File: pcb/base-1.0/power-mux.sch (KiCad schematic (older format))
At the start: 23 parts, among them Q201 IRF7324, Q202 IRF7324, Q203 IRF7324, U201 LTC4417

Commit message: o Replacing footprints with IPC footprints.
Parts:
- C201, C202, C203, C204, C205, C206: footprint Capacitor_SMD:C_0402_1005Metric -> IPC-7351-CAPC:CAPC_1005x015
- R201, R202, R203, R204, R205, R206, R207, R208, R209, R210, R211, R212: footprint Resistor_SMD:R_0402_1005Metric -> IPC-7351-RESC:RESC_1005x015

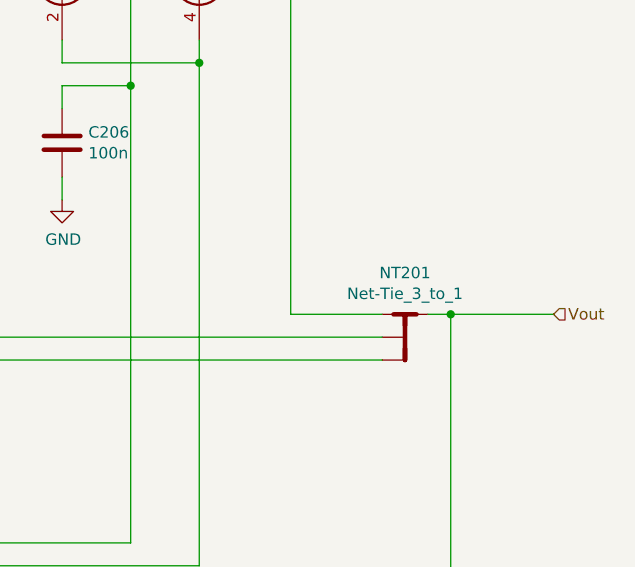
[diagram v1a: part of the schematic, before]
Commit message: o Better symbol for BC817, Q101 and Q102. o Adding footprint for jack, J104.
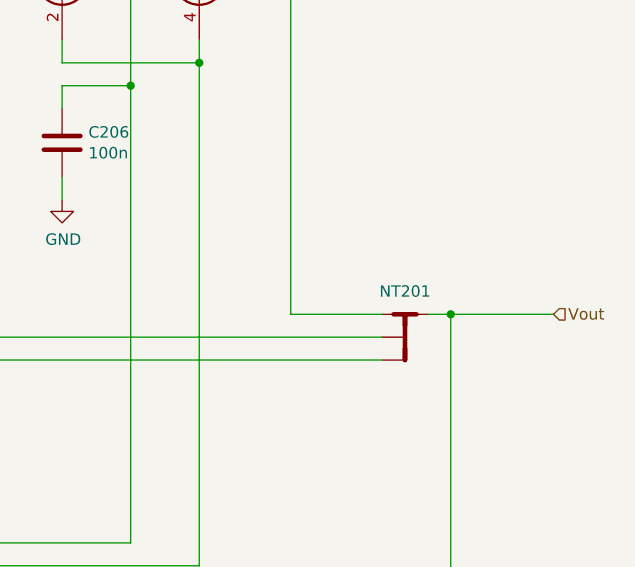
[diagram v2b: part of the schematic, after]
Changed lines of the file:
@@
 U 1 1 5D02029B
 P 10000 3400
-F 0 "NT201" H 10000 3581 50  0000 C CNN
-F 1 "Net-Tie_3_to_1" H 10000 3490 50  0000 C CNN
+F 0 "NT201" H 10000 3500 50  0000 C CNN
+F 1 "Net-Tie_3_to_1" H 10000 3490 50  0001 C CNN
 F 2 "NetTie:NetTie-4_SMD_Pad0.5mm" H 10000 3400 50  0001 C CNN
 F 3 "~" H 10000 3400 50  0001 C CNN

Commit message: o Selecting parts.
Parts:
- C201, C202, C203, C204, C205, C206: value 100n -> 100nF; mpn (none) -> CL05B104KO5NNNC
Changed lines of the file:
@@
 P 8500 2650
 F 0 "C206" H 8615 2696 50  0000 L CNN
-F 1 "100n" H 8615 2605 50  0000 L CNN
+F 1 "100nF" H 8615 2605 50  0000 L CNN
 F 2 "IPC-7351-CAPC:CAPC_1005x015" H 8538 2500 50  0001 C CNN
 F 3 "~" H 8500 2650 50  0001 C CNN
+F 4 "CL05B104KO5NNNC" H 8500 2650 50  0001 C CNN "mpn"
 	1    8500 2650
 	1    0    0    -1
@@
 P 2300 1600
 F 0 "C202" H 2415 1646 50  0000 L CNN
-F 1 "100n" H 2415 1555 50  0000 L CNN
+F 1 "100nF" H 2415 1555 50  0000 L CNN
 F 2 "IPC-7351-CAPC:CAPC_1005x015" H 2338 1450 50  0001 C CNN
 F 3 "~" H 2300 1600 50  0001 C CNN
+F 4 "CL05B104KO5NNNC" H 2300 1600 50  0001 C CNN "mpn"
 	1    2300 1600
 	1    0    0    -1
@@
 P 1600 1600
 F 0 "C201" H 1715 1646 50  0000 L CNN
-F 1 "100n" H 1715 1555 50  0000 L CNN
+F 1 "100nF" H 1715 1555 50  0000 L CNN
 F 2 "IPC-7351-CAPC:CAPC_1005x015" H 1638 1450 50  0001 C CNN
 F 3 "~" H 1600 1600 50  0001 C CNN
+F 4 "CL05B104KO5NNNC" H 1600 1600 50  0001 C CNN "mpn"
 	1    1600 1600
 	1    0    0    -1
@@
 P 3000 1600
 F 0 "C203" H 3115 1646 50  0000 L CNN
-F 1 "100n" H 3115 1555 50  0000 L CNN
+F 1 "100nF" H 3115 1555 50  0000 L CNN
 F 2 "IPC-7351-CAPC:CAPC_1005x015" H 3038 1450 50  0001 C CNN
 F 3 "~" H 3000 1600 50  0001 C CNN
+F 4 "CL05B104KO5NNNC" H 3000 1600 50  0001 C CNN "mpn"
 	1    3000 1600
 	1    0    0    -1
@@
 P 6700 2650
 F 0 "C205" H 6815 2696 50  0000 L CNN
-F 1 "100n" H 6815 2605 50  0000 L CNN
+F 1 "100nF" H 6815 2605 50  0000 L CNN
 F 2 "IPC-7351-CAPC:CAPC_1005x015" H 6738 2500 50  0001 C CNN
 F 3 "~" H 6700 2650 50  0001 C CNN
+F 4 "CL05B104KO5NNNC" H 6700 2650 50  0001 C CNN "mpn"
 	1    6700 2650
 	1    0    0    -1
@@
 P 4900 2650
 F 0 "C204" H 5015 2696 50  0000 L CNN
-F 1 "100n" H 5015 2605 50  0000 L CNN
+F 1 "100nF" H 5015 2605 50  0000 L CNN
 F 2 "IPC-7351-CAPC:CAPC_1005x015" H 4938 2500 50  0001 C CNN
 F 3 "~" H 4900 2650 50  0001 C CNN
+F 4 "CL05B104KO5NNNC" H 4900 2650 50  0001 C CNN "mpn"
 	1    4900 2650
 	1    0    0    -1

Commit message: o Selecting parts.
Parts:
- Q201, Q202, Q203: value IRF7324 -> IRF7324TRPBF; mpn (none) -> IRF7324TRPBF
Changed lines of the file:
@@
 P 9100 2000
 F 0 "Q203" V 9525 2000 50  0000 C CNN
-F 1 "IRF7324" V 9434 2000 50  0000 C CNN
+F 1 "IRF7324TRPBF" V 9434 2000 50  0000 C CNN
 F 2 "Package_SO:PowerIntegrations_SO-8" H 9150 2000 50  0001 C CNN
-F 3 "~" H 9150 2000 50  0001 C CNN
+F 3 "https://www.infineon.com/dgdl/irf7324pbf.pdf?fileId=5546d462533600a4015355f5f0861b4b" H 9150 2000 50  0001 C CNN
+F 4 "IRF7324TRPBF" H 9100 2000 50  0001 C CNN "mpn"
 	2    9100 2000
 	0    1    -1   0
@@
 P 8500 2000
 F 0 "Q203" V 8925 2000 50  0000 C CNN
-F 1 "IRF7324" V 8834 2000 50  0000 C CNN
+F 1 "IRF7324TRPBF" V 8834 2000 50  0000 C CNN
 F 2 "Package_SO:PowerIntegrations_SO-8" H 8550 2000 50  0001 C CNN
-F 3 "~" H 8550 2000 50  0001 C CNN
+F 3 "https://www.infineon.com/dgdl/irf7324pbf.pdf?fileId=5546d462533600a4015355f5f0861b4b" H 8550 2000 50  0001 C CNN
+F 4 "IRF7324TRPBF" H 8500 2000 50  0001 C CNN "mpn"
 	1    8500 2000
 	0    -1   -1   0
@@
 P 7300 2000
 F 0 "Q202" V 7725 2000 50  0000 C CNN
-F 1 "IRF7324" V 7634 2000 50  0000 C CNN
+F 1 "IRF7324TRPBF" V 7634 2000 50  0000 C CNN
 F 2 "Package_SO:PowerIntegrations_SO-8" H 7350 2000 50  0001 C CNN
-F 3 "~" H 7350 2000 50  0001 C CNN
+F 3 "https://www.infineon.com/dgdl/irf7324pbf.pdf?fileId=5546d462533600a4015355f5f0861b4b" H 7350 2000 50  0001 C CNN
+F 4 "IRF7324TRPBF" H 7300 2000 50  0001 C CNN "mpn"
 	2    7300 2000
 	0    1    -1   0
@@
 P 6700 2000
 F 0 "Q202" V 7125 2000 50  0000 C CNN
-F 1 "IRF7324" V 7034 2000 50  0000 C CNN
+F 1 "IRF7324TRPBF" V 7034 2000 50  0000 C CNN
 F 2 "Package_SO:PowerIntegrations_SO-8" H 6750 2000 50  0001 C CNN
-F 3 "~" H 6750 2000 50  0001 C CNN
+F 3 "https://www.infineon.com/dgdl/irf7324pbf.pdf?fileId=5546d462533600a4015355f5f0861b4b" H 6750 2000 50  0001 C CNN
+F 4 "IRF7324TRPBF" H 6700 2000 50  0001 C CNN "mpn"
 	1    6700 2000
 	0    -1   -1   0
@@
 P 5500 2000
 F 0 "Q201" V 5925 2000 50  0000 C CNN
-F 1 "IRF7324" V 5834 2000 50  0000 C CNN
+F 1 "IRF7324TRPBF" V 5834 2000 50  0000 C CNN
 F 2 "Package_SO:PowerIntegrations_SO-8" H 5550 2000 50  0001 C CNN
-F 3 "~" H 5550 2000 50  0001 C CNN
+F 3 "https://www.infineon.com/dgdl/irf7324pbf.pdf?fileId=5546d462533600a4015355f5f0861b4b" H 5550 2000 50  0001 C CNN
+F 4 "IRF7324TRPBF" H 5500 2000 50  0001 C CNN "mpn"
 	2    5500 2000
 	0    1    -1   0
@@
 P 4900 2000
 F 0 "Q201" V 5325 2000 50  0000 C CNN
-F 1 "IRF7324" V 5234 2000 50  0000 C CNN
+F 1 "IRF7324TRPBF" V 5234 2000 50  0000 C CNN
 F 2 "Package_SO:PowerIntegrations_SO-8" H 4950 2000 50  0001 C CNN
-F 3 "~" H 4950 2000 50  0001 C CNN
+F 3 "https://www.infineon.com/dgdl/irf7324pbf.pdf?fileId=5546d462533600a4015355f5f0861b4b" H 4950 2000 50  0001 C CNN
+F 4 "IRF7324TRPBF" H 4900 2000 50  0001 C CNN "mpn"
 	1    4900 2000
 	0    -1   -1   0

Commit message: o Much more PCB work.
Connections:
- net Vin_PoE_sel: now reaches NT201.1, Q203.5 (D), Q203.6 (D)
- net Vin_adapter_sel: now reaches NT201.2, Q202.5 (D), Q202.6 (D)
- net Vin_USB_sel: now reaches NT201.3, Q201.5 (D), Q201.6 (D)
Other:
- moved on the sheet: NT201
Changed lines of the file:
@@
 TODO:\n* Select MOSFETs. One option: CSD75207W15\n* Calculate resistor values
 Wire Wire Line
-	6500 5500 10200 5500
+	6500 5500 10550 5500
 Connection ~ 5900 1900
 Wire Wire Line
@@
 	9300 1800 9500 1800
 Wire Wire Line
-	9500 3400 9900 3400
+	9500 3400 10250 3400
 Wire Wire Line
 	9500 1900 9500 3400
@@
 Text HLabel 1100 800  0    50   Input ~ 0
 Vin_PoE
-Text HLabel 10650 3400 2    50   Input ~ 0
+Text HLabel 10750 3400 2    50   Input ~ 0
 Vout
 Wire Wire Line
-	10200 3400 10650 3400
-Connection ~ 10200 3400
-Wire Wire Line
-	10100 3400 10200 3400
+	10550 3400 10750 3400
+Connection ~ 10550 3400
+Wire Wire Line
+	10450 3400 10550 3400
 $Comp
 L unlockoslo:Net-Tie_3_to_1 NT201
 U 1 1 5D02029B
-P 10000 3400
-F 0 "NT201" H 10000 3500 50  0000 C CNN
-F 1 "Net-Tie_3_to_1" H 10000 3490 50  0001 C CNN
-F 2 "NetTie:NetTie-4_SMD_Pad0.5mm" H 10000 3400 50  0001 C CNN
-F 3 "~" H 10000 3400 50  0001 C CNN
-	1    10000 3400
-	1    0    0    -1
-$EndComp
-Wire Wire Line
-	10200 5500 10200 3400
+P 10350 3400
+F 0 "NT201" H 10350 3500 50  0000 C CNN
+F 1 "Net-Tie_3_to_1" H 10350 3490 50  0001 C CNN
+F 2 "NetTie:NetTie-4_SMD_Pad0.5mm" H 10350 3400 50  0001 C CNN
+F 3 "~" H 10350 3400 50  0001 C CNN
+	1    10350 3400
+	1    0    0    -1
+$EndComp
+Wire Wire Line
+	10550 5500 10550 3400
 Connection ~ 1400 2200
 Wire Wire Line
@@
 	4600 5000 4600 4100
 Wire Wire Line
-	7700 3500 9900 3500
-Wire Wire Line
-	5900 3600 9900 3600
+	7700 3500 10250 3500
+Wire Wire Line
+	5900 3600 10250 3600
 Wire Wire Line
 	7700 1900 7700 3500
@@
 Wire Wire Line
 	5100 1900 5200 1900
+Text Label 10250 3600 2    50   ~ 0
+Vin_USB_sel
+Text Label 10250 3500 2    50   ~ 0
+Vin_adapter_sel
+Text Label 10250 3400 2    50   ~ 0
+Vin_PoE_sel
 $EndSCHEMATC

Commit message: o More PCB work.
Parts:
- removed NT201: Net-Tie_3_to_1, NetTie:NetTie-4_SMD_Pad0.5mm, symbol unlockoslo:Net-Tie_3_to_1
- added NT301, NT302: Net-Tie_3, UnlockOslo:NetTie-3_SMD_Pad0.5mm_132, symbol Device:Net-Tie_3
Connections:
- net Vin_PoE_sel: now also NT302.1
- net Vin_USB_sel: now also NT301.3
- net Vin_adapter_sel: now also NT301.1
- net Vout: now also NT302.2
- net UV3: now reaches R201.2, R202.1, U201.8 (UV3)
- net OV3: now reaches R202.2, R203.1, U201.9 (OV3)
- net UV2: now reaches R204.2, R205.1, U201.6 (UV2)
- net OV2: now reaches R205.2, R206.1, U201.7 (OV2)
- net UV1: now reaches R207.2, R208.1, U201.4 (UV1)
- net OV1: now reaches R208.2, R209.1, U201.5 (OV1)
- new net: NT301.2, NT302.3
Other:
- moved on the sheet: C201, C202, C203, C204, C205, C206, Q201A, Q201B, Q202A, Q202B, Q203A, Q203B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

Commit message: o 4 layers.
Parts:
- removed NT301, NT302: Net-Tie_3, UnlockOslo:NetTie-3_SMD_Pad0.5mm_132, symbol Device:Net-Tie_3
- added NT201: Net-Tie_3_to_1, NetTie:NetTie-4_SMD_Pad0.5mm, symbol unlockoslo:Net-Tie_3_to_1
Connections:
- net Vin_PoE_sel: now also NT201.1
- net Vin_USB_sel: now also NT201.3
- net Vin_adapter_sel: now also NT201.2
- net Vout: now also NT201.4
- net OV1: no longer names the net of R208.2, R209.1, U201.5 (OV1)
- net OV2: no longer names the net of R205.2, R206.1, U201.7 (OV2)
- net OV3: no longer names the net of R202.2, R203.1, U201.9 (OV3)
- net UV1: no longer names the net of R207.2, R208.1, U201.4 (UV1)
- net UV2: no longer names the net of R204.2, R205.1, U201.6 (UV2)
- net UV3: no longer names the net of R201.2, R202.1, U201.8 (UV3)
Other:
- note added: "TODO:\n* Calculate resistor values"
- note removed: "TODO:\n* Select MOSFETs. One option: CSD75207W15\n* Calculate resistor values"
- moved on the sheet: C201, C202, C203, C204, C205, C206, Q201A, Q201B, Q202A, Q202B, Q203A, Q203B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

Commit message: o More PCB work.
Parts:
- removed NT201: Net-Tie_3_to_1, NetTie:NetTie-4_SMD_Pad0.5mm, symbol unlockoslo:Net-Tie_3_to_1
- added NT1, NT2: Net-Tie_3, UnlockOslo:NetTie-3_SMD_Pad0.5mm_132, symbol Device:Net-Tie_3
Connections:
- net Vin_PoE_sel: now also NT1.1
- net Vin_USB_sel: now also NT2.3
- net Vin_adapter_sel: now also NT2.1
- net Vout: now also NT1.2
- new net: NT1.3, NT2.2
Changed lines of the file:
@@
 TODO:\n* Calculate resistor values
 Wire Wire Line
-	6500 5500 10550 5500
+	6500 5500 10750 5500
 Connection ~ 5900 1900
 Wire Wire Line
@@
 Wire Wire Line
 	9300 1800 9500 1800
-Wire Wire Line
-	9500 3400 10250 3400
 Wire Wire Line
 	9500 1900 9500 3400
@@
 Text HLabel 1100 800  0    50   Input ~ 0
 Vin_PoE
-Text HLabel 10750 3400 2    50   Input ~ 0
+Text HLabel 10950 3400 2    50   Input ~ 0
 Vout
 Wire Wire Line
-	10550 3400 10750 3400
-Connection ~ 10550 3400
-Wire Wire Line
-	10450 3400 10550 3400
-$Comp
-L unlockoslo:Net-Tie_3_to_1 NT201
-U 1 1 5D02029B
-P 10350 3400
-F 0 "NT201" H 10350 3500 50  0000 C CNN
-F 1 "Net-Tie_3_to_1" H 10350 3490 50  0001 C CNN
-F 2 "NetTie:NetTie-4_SMD_Pad0.5mm" H 10350 3400 50  0001 C CNN
-F 3 "~" H 10350 3400 50  0001 C CNN
-	1    10350 3400
-	1    0    0    -1
-$EndComp
-Wire Wire Line
-	10550 5500 10550 3400
+	10750 3400 10950 3400
+Connection ~ 10750 3400
+Wire Wire Line
+	10750 5500 10750 3400
 Connection ~ 1400 2200
 Wire Wire Line
@@
 	4600 5000 4600 4100
 Wire Wire Line
-	7700 3500 10250 3500
-Wire Wire Line
-	5900 3600 10250 3600
+	7700 3500 10050 3500
+Wire Wire Line
+	5900 3600 10050 3600
 Wire Wire Line
 	7700 1900 7700 3500
@@
 Wire Wire Line
 	5100 1900 5200 1900
-Text Label 10250 3600 2    50   ~ 0
+Text Label 10050 3600 2    50   ~ 0
 Vin_USB_sel
-Text Label 10250 3500 2    50   ~ 0
+Text Label 10050 3500 2    50   ~ 0
 Vin_adapter_sel
-Text Label 10250 3400 2    50   ~ 0
+Text Label 10050 3400 2    50   ~ 0
 Vin_PoE_sel
+$Comp
+L Device:Net-Tie_3 NT2
+U 1 1 5D13BBF9
+P 10150 3500
+F 0 "NT2" H 10150 3311 50  0000 C CNN
+F 1 "Net-Tie_3" H 10150 3590 50  0001 C CNN
+F 2 "UnlockOslo:NetTie-3_SMD_Pad0.5mm_132" H 10150 3500 50  0001 C CNN
+F 3 "~" H 10150 3500 50  0001 C CNN
+	1    10150 3500
+	1    0    0    -1
+$EndComp
+$Comp
+L Device:Net-Tie_3 NT1
+U 1 1 5D13CB32
+P 10450 3400
+F 0 "NT1" H 10450 3489 50  0000 C CNN
+F 1 "Net-Tie_3" H 10450 3490 50  0001 C CNN
+F 2 "UnlockOslo:NetTie-3_SMD_Pad0.5mm_132" H 10450 3400 50  0001 C CNN
+F 3 "~" H 10450 3400 50  0001 C CNN
+	1    10450 3400
+	1    0    0    -1
+$EndComp
+Wire Wire Line
+	10550 3400 10750 3400
+Wire Wire Line
+	9500 3400 10350 3400
+Wire Wire Line
+	10250 3500 10350 3500
 $EndSCHEMATC
